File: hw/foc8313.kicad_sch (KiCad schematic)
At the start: 36 parts, among them P1 USB_C_Plug_USB2.0, SW1 SW_SPST, U1 DRV8313PWP, U2 STM32F103CBTx, U3 INA240A3D, U4 AS5047D, U5 MP2456, U6 SN65HVD230

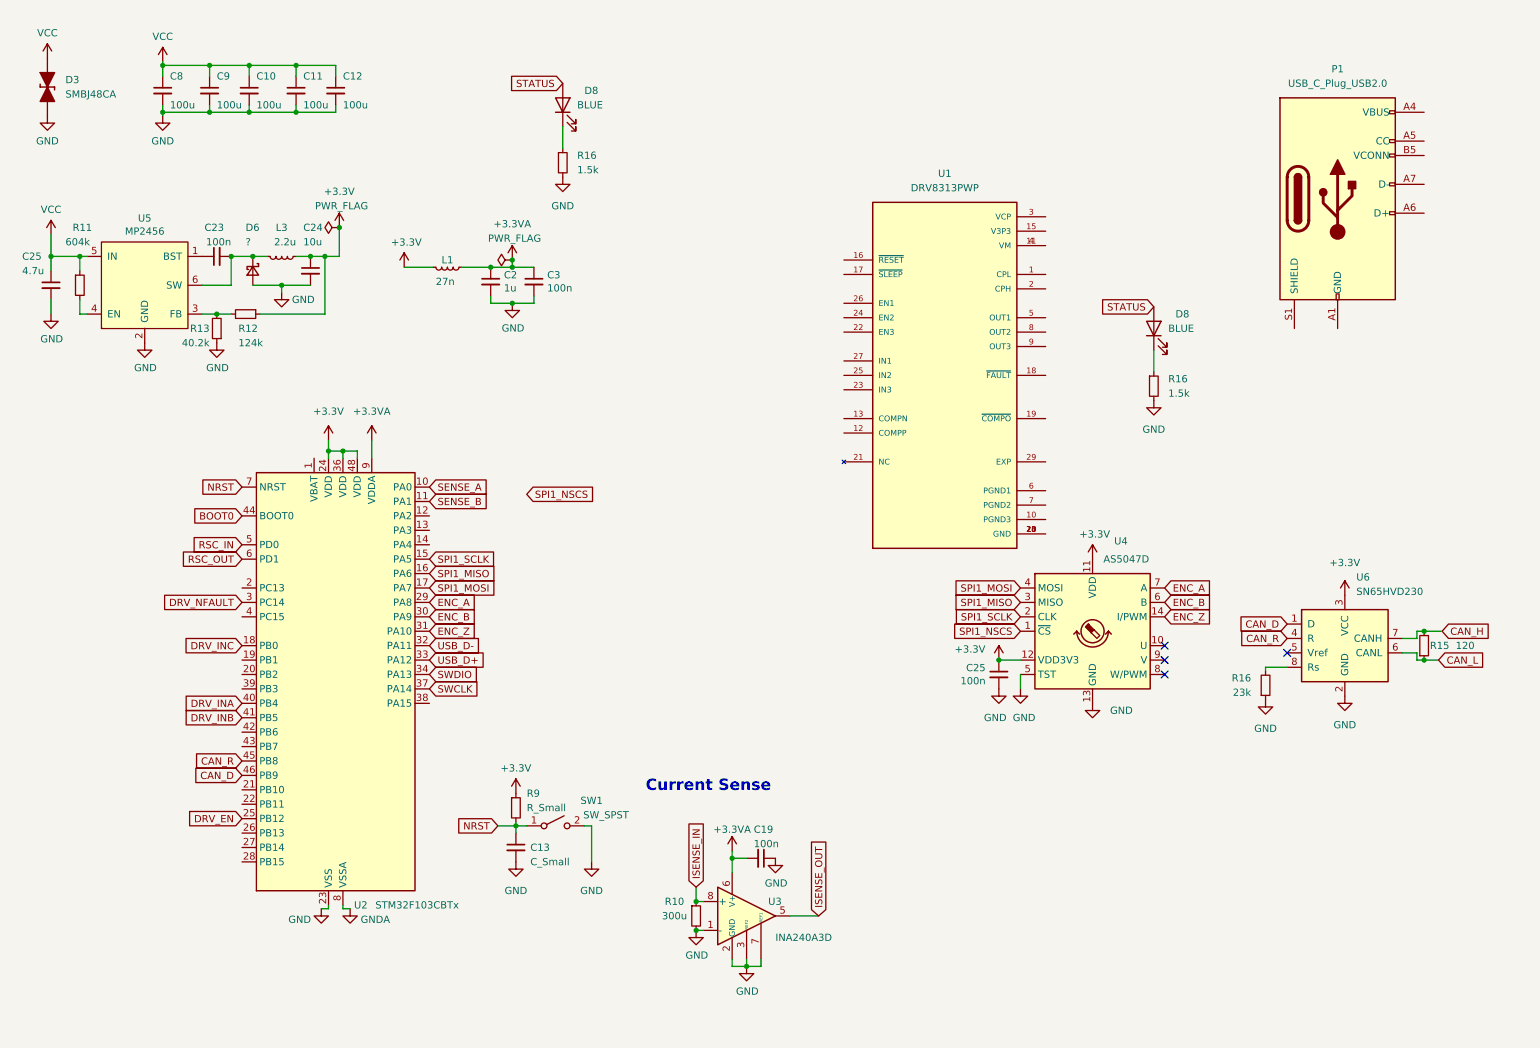
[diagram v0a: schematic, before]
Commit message: [Hw] 5V buck, Isocan, Encoder, MCU, with LCSC parts
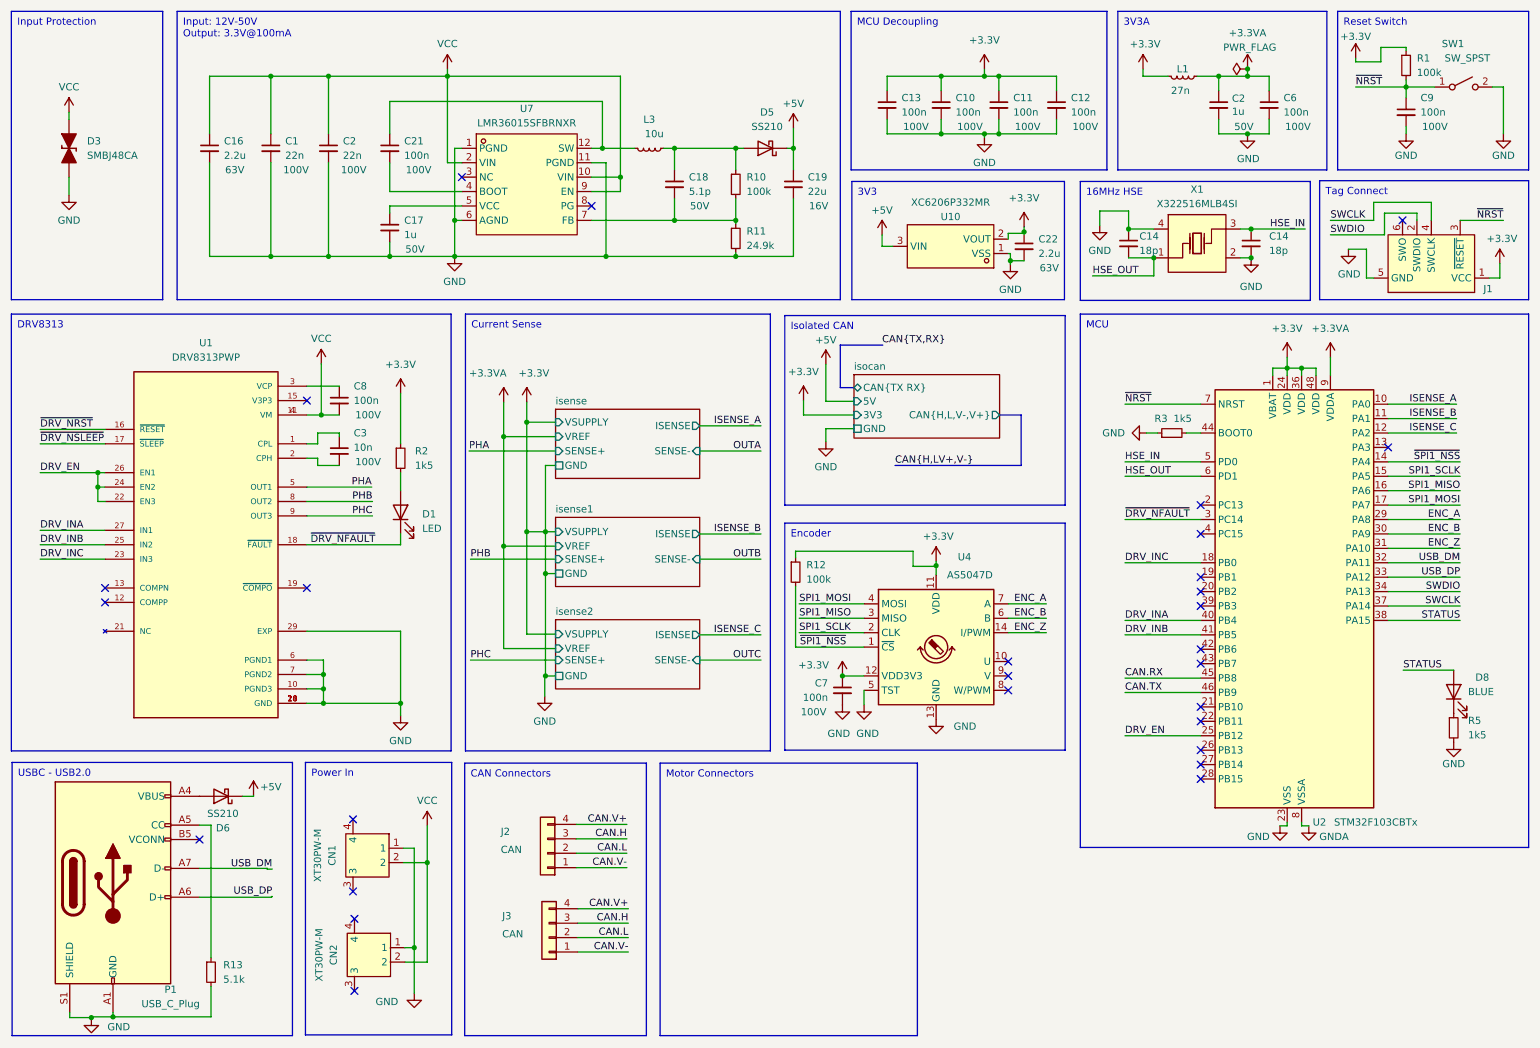
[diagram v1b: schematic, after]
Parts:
- removed C23, C25: 100n, Capacitor_SMD:C_0603_1608Metric, symbol Device:C_Small
- removed C24: 10u, Capacitor_SMD:C_0603_1608Metric, symbol Device:C_Small
- removed C25: 4.7u, Capacitor_SMD:C_0603_1608Metric, symbol Device:C_Small
- removed D6: ?, Diode_SMD:D_0603_1608Metric, symbol Device:D_Schottky_Small
- removed D8: BLUE, LED_SMD:LED_0603_1608Metric, symbol Device:LED
- removed R15: 120, Resistor_SMD:R_0805_2012Metric, symbol Device:R_Small
- removed R16: 23k, Resistor_SMD:R_0603_1608Metric, symbol Device:R_Small
- removed R16 (x2): 1.5k, Resistor_SMD:R_0603_1608Metric, symbol Device:R_Small
- removed R9: R_Small, symbol Device:R_Small
- removed U3: INA240A3D, Package_SO:SOIC-8_3.9x4.9mm_P1.27mm, symbol Amplifier_Current:INA240A3D
- removed U5: MP2456, Package_TO_SOT_SMD:TSOT-23-6, symbol MP2456:MP2456
- removed U6: SN65HVD230, Package_SO:SOIC-8_3.9x4.9mm_P1.27mm, symbol Interface_CAN_LIN:SN65HVD230
- added C1, C2: 22n, Capacitor_SMD:C_0603_1608Metric, symbol Device:C_Small
- added C14 (x2): 18p, Capacitor_SMD:C_0402_1005Metric, symbol Device:C_Small
- added C16, C22: 2.2u, Capacitor_SMD:C_0805_2012Metric, symbol Device:C_Small
- added C17: 1u, Capacitor_SMD:C_0603_1608Metric, symbol Device:C_Small
- added C18: 5.1p, Capacitor_SMD:C_0603_1608Metric, symbol Device:C_Small
- added C21, C6, C7: 100n, Capacitor_SMD:C_0603_1608Metric, symbol Device:C_Small
- added CN1, CN2: XT30PW-M, easyeda:CONN-TH_XT30PW-M, symbol easyeda:XT30PW-M
- added D1: LED, Diode_SMD:D_0603_1608Metric, symbol Device:LED
- added D5, D6: SS210, Diode_SMD:D_SMA, symbol Device:D_Schottky
- added J1: Tag Connect, Connector:Tag-Connect_TC2030-IDC-NL_2x03_P1.27mm_Vertical, symbol Connector:Conn_ARM_SWD_TagConnect_TC2030-NL
- added J2, J3: CAN, Connector_JST:JST_GH_SM04B-GHS-TB_1x04-1MP_P1.25mm_Horizontal, symbol Connector_Generic:Conn_01x04
- added R1: 100k, Resistor_SMD:R_0603_1608Metric, symbol Device:R_Small
- added R2, R3, R5: 1k5, Resistor_SMD:R_0603_1608Metric, symbol Device:R_Small
- added U10: XC6206P332MR, easyeda:SOT-23-3_L3.0-W1.7-P0.95-LS2.9-BR, symbol easyeda:XC6206P332MR_C347376
- added U7: LMR36015SFBRNXR, easyeda:VQFN-12_L3.0-W2.0-P0.65-BL_TI_RNX, symbol easyeda:LMR36015SFBRNXR
- added X1: X322516MLB4SI, easyeda:OSC-SMD_4P-L3.2-W2.5-BL, symbol easyeda:X322516MLB4SI
- C10, C11, C12, C8, C9: value 100u -> 100n; footprint (none) -> Capacitor_SMD:C_0603_1608Metric; LCSC (none) -> C15725; Rating (none) -> 100V
- C13: value C_Small -> 100n; footprint (none) -> Capacitor_SMD:C_0603_1608Metric; LCSC (none) -> C15725; Rating (none) -> 100V
- C19: value 100n -> 22u; footprint Capacitor_SMD:C_0603_1608Metric -> Resistor_SMD:R_0805_2012Metric; LCSC (none) -> C98190; Rating (none) -> 16V
- C2: LCSC (none) -> C15849; Rating (none) -> 50V
- C3: value 100n -> 10n; LCSC (none) -> C302008; Rating (none) -> 100V
- D8: LCSC (none) -> C19189746
- L1: LCSC (none) -> C280267
- L3: value 2.2u -> 10u; footprint Inductor_SMD:L_0603_1608Metric -> Inductor_SMD:L_0805_2012Metric; LCSC (none) -> C285963
- P1: value USB_C_Plug_USB2.0 -> USB_C_Plug; footprint (none) -> easyeda:USB-3.1-SMD_USB3.1-TYPE-C-FSABC
- R10: value 300u -> 100k; footprint Resistor_SMD:R_2512_6332Metric -> Resistor_SMD:R_0603_1608Metric; LCSC (none) -> C25803
- R11: value 604k -> 24.9k; LCSC (none) -> C25962
- R12: value 124k -> 100k; LCSC (none) -> C25803
- R13: value 40.2k -> 5.1k; LCSC (none) -> C23186
- U1: footprint SOP65P640X120-29N -> easyeda:HTSSOP-28_L9.8-W4.5-P0.65-LS6.6-BL-EP; LCSC (none) -> C92482
- U2: LCSC (none) -> C8304
- U4: LCSC (none) -> C962063
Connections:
- net DRV_NFAULT is gone; now on net ~{DRV_NFAULT}: U2.3 (PC14)
- net SPI1_NSCS is gone; now on net ~{SPI1_NSS}: U4.1 (~{CS})
- net USB_D+ is gone; now on net USB_DP: U2.33 (PA12)
- net USB_D- is gone; now on net USB_DM: U2.32 (PA11)
- net +3.3V: now also C10.1, C10.2, C11.1, C11.2, C12.1, C12.2, C13.1, C13.2, C19.2, C2.2, C9.2, D3.1 (K), P1.A1 (GND), P1.A12 (GND), P1.B1 (GND), P1.B12 (GND), P1.S1 (SHIELD), R11.2, R13.2, SW1.2 (B), U1.10 (PGND3), U1.14 (GND), U1.20 (GND), U1.28 (GND), U1.29 (EXP), U1.6 (PGND1), U1.7 (PGND2), U2.1 (VBAT), U2.23 (VSS), U2.35 (VSS), U2.47 (VSS), U4.13 (GND), U4.5 (TST), C1.2, C14.1, C14.2, C16.2, C17.2, C2.2, C22.1, C22.2, C6.2, C7.2, CN1.1, CN2.1, J1.5 (GND), R1.1, R2.1, R3.1, R5.2, U10.1 (VSS), U10.2 (VOUT), U7.1 (PGND), U7.11 (PGND), U7.6 (AGND), X1.2, X1.4
- net +3.3VA: now also C6.1; no longer C19.2, C3.1
- net +3V3: now also C7.1, J1.1 (VCC); no longer L3.1
- net DRV_EN: now also U1.22 (EN3), U1.24 (EN2), U1.26 (EN1)
- net DRV_INA: now also U1.27 (IN1)
- net DRV_INB: now also U1.25 (IN2)
- net DRV_INC: now also U1.23 (IN3)
- net STATUS: now also U2.38 (PA15)
- net SWCLK: now also J1.4 (SWCLK)
- net SWDIO: now also J1.2 (SWDIO)
- net VCC: now also C8.2, U1.11 (VM), U1.4 (VM), C1.1, C16.1, C2.1, CN1.2, CN2.2, U7.10 (VIN), U7.2 (VIN), U7.9 (EN); no longer C10.1, C11.1, C12.1, C8.1, C9.1, R11.1
- net ~{SPI1_NSS}: now reaches R12.2
- net ~{SPI1_NSS}: now also U2.14 (PA4); no longer R13.2
- net ISENSE_C: now reaches U2.12 (PA2)
- net at L3.2: now also C21.1, U7.12 (SW)
- net at D8.1 (K): now also R5.1
- net at U1.1 (CPL): now also C3.1
- net ~{DRV_NRST}: now reaches U1.16 (~{RESET})
- net ~{DRV_NSLEEP}: now reaches U1.17 (~{SLEEP})
- net ~{DRV_NFAULT}: now reaches U1.18 (~{FAULT})
- net ~{DRV_NFAULT}: now also D1.1 (K)
- net at U1.2 (CPH): now also C3.2
- net at U1.3 (VCP): now also C8.1
- net PHA: now reaches U1.5 (OUT1)
- net PHB: now reaches U1.8 (OUT2)
- net PHC: now reaches U1.9 (OUT3)
- net at P1.A4 (VBUS), P1.A9 (VBUS), P1.B4 (VBUS)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: now also D6.2 (A)
- net at P1.A5 (CC): now also R13.1
- net USB_DP: now reaches P1.A6 (D+)
- net USB_DM: now reaches P1.A7 (D-)
- net BOOT0: no longer names the net of U2.44 (BOOT0)
- net BOOT0: now also R3.2
- net CAN_D renamed CAN.TX
- net CAN_R renamed CAN.RX
- removed net GND: C10.2, C11.2, C12.2, C13.2, C19.1, C2.2, C3.2, C8.2, C9.2, D3.1 (K), R10.2, R13.1, SW1.2 (B), U2.23 (VSS), U2.35 (VSS), U2.47 (VSS), U4.13 (GND), U4.5 (TST)
- net ISENSE_IN: no longer names the net of R10.1
- net ISENSE_IN: now also L3.1, C18.1, D5.2 (A)
- net NRST renamed ~{NRST}
- net ~{NRST}: now also C9.1, J1.3 (~{RESET}), R1.2; no longer C13.1
- net RSC_IN renamed HSE_IN
- net HSE_IN: now also C14.1, X1.3
- net RSC_OUT renamed HSE_OUT
- net HSE_OUT: now also C14.2, X1.1
- net SENSE_A renamed ISENSE_A
- net SENSE_B renamed ISENSE_B
- new net: C18.2, R10.2, R11.1, U7.7 (FB)
- new net: C17.1, U7.5 (VCC)
- new net: D1.2 (A), R2.2
- new net: C21.2, U7.4 (BOOT)
- new net +5V: C19.1, D5.1 (K), D6.1 (K), U10.3 (VIN)
- new net CAN.H: J2.3 (Pin_3), J3.3 (Pin_3)
- new net CAN.L: J2.2 (Pin_2), J3.2 (Pin_2)
- new net CAN.V+: J2.4 (Pin_4), J3.4 (Pin_4)
- new net CAN.V-: J2.1 (Pin_1), J3.1 (Pin_1)
- no-connect marks 4 -> 28
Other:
- added sheet isense (isense.kicad_sch)
- added sheet isense1 (isense.kicad_sch)
- added sheet isense2 (isense.kicad_sch)
- added sheet isocan (isocan.kicad_sch)
- note removed: "Current Sense"
- moved on the sheet: C2, D3, D8, L1, SW1, U1, U2, U4

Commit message: WIP XT30?
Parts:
- removed J3: CAN, Connector_JST:JST_GH_SM04B-GHS-TB_1x04-1MP_P1.25mm_Horizontal, symbol Connector_Generic:Conn_01x04
- added J3: CAN, Connector_JST:JST_GH_SM03B-GHS-TB_1x03-1MP_P1.25mm_Horizontal, symbol Connector_Generic:Conn_01x03
- added U6: MR30PW-M30.G.Y, easyeda:CONN-TH_MR30PW-M30-G-Y, symbol easyeda:MR30PW-M30.G.Y
- J2: footprint Connector_JST:JST_GH_SM04B-GHS-TB_1x04-1MP_P1.25mm_Horizontal -> Connector_JST:JST_GH_SM03B-GHS-TB_1x03-1MP_P1.25mm_Horizontal; symbol Connector_Generic:Conn_01x04 -> Connector_Generic:Conn_01x03; LCSC Part C3029379 -> C514175
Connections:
- net +3.3V: no longer C1.2, C10.2, C11.2, C12.2, C13.2, C14.1, C14.2, C16.2, C17.2, C19.2, C2.2, C2.2, C22.2, C6.2, C7.2, C9.2, CN1.1, CN2.1, D3.1 (K), J1.5 (GND), P1.A1 (GND), P1.A12 (GND), P1.B1 (GND), P1.B12 (GND), P1.S1 (SHIELD), R11.2, R13.2, R3.1, R5.2, SW1.2 (B), U1.10 (PGND3), U1.14 (GND), U1.20 (GND), U1.28 (GND), U1.29 (EXP), U1.6 (PGND1), U1.7 (PGND2), U10.1 (VSS), U2.23 (VSS), U2.35 (VSS), U2.47 (VSS), U4.13 (GND), U4.5 (TST), U7.1 (PGND), U7.11 (PGND), U7.6 (AGND), X1.2, X1.4
- net CAN.H: now also J3.3 (Pin_3)
- net CAN.L: now also J3.2 (Pin_2)
- net CAN.V-: now also J3.1 (Pin_1)
- net OUTA: now also U6.1
- net OUTB: now also U6.2
- net OUTC: now also U6.3
- net VCC: now also CN1.1, CN2.1; no longer CN1.2, CN2.2
- removed net CAN.V+: J2.4 (Pin_4)
- new net GND: C1.2, C10.2, C11.2, C12.2, C13.2, C14.1, C14.2, C16.2, C17.2, C19.2, C2.2, C2.2, C22.2, C6.2, C7.2, C9.2, CN1.2, CN2.2, D3.1 (K), J1.5 (GND), P1.A1 (GND), P1.A12 (GND), P1.B1 (GND), P1.B12 (GND), P1.S1 (SHIELD), R11.2, R13.2, R3.1, R5.2, SW1.2 (B), U1.10 (PGND3), U1.14 (GND), U1.20 (GND), U1.28 (GND), U1.29 (EXP), U1.6 (PGND1), U1.7 (PGND2), U10.1 (VSS), U2.23 (VSS), U2.35 (VSS), U2.47 (VSS), U4.13 (GND), U4.5 (TST), U7.1 (PGND), U7.11 (PGND), U7.6 (AGND), X1.2, X1.4
- no-connect marks 28 -> 30

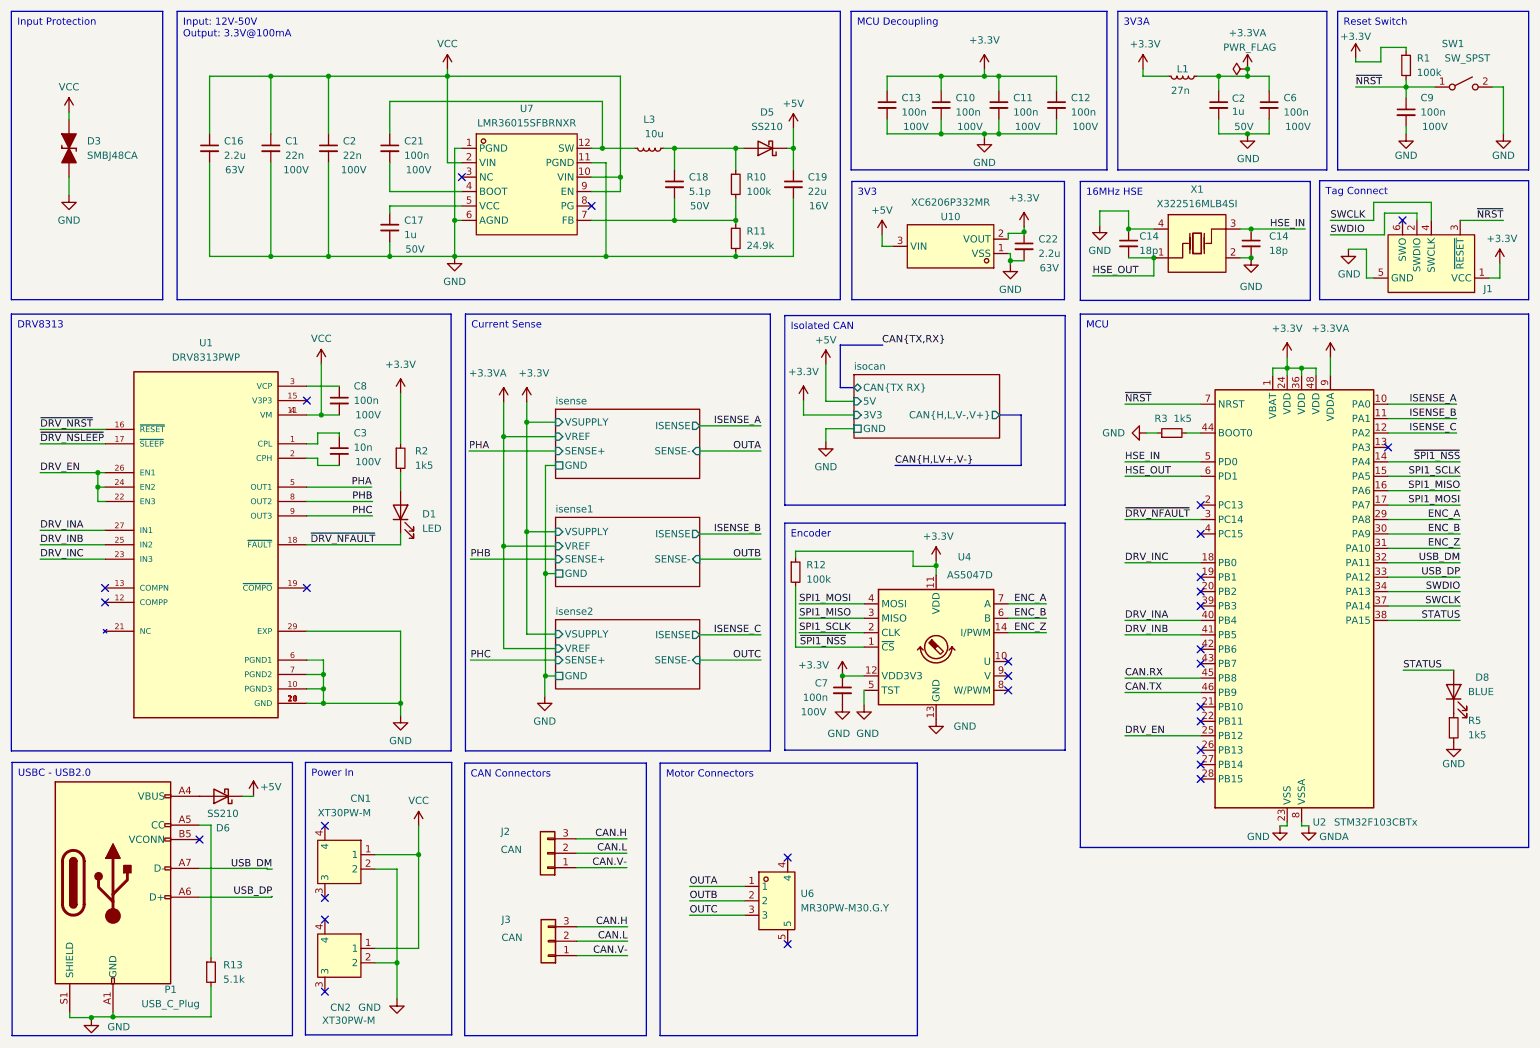
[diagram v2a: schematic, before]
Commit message: [Hw] No iso can, 0402 where possible, approx layout and formfactor
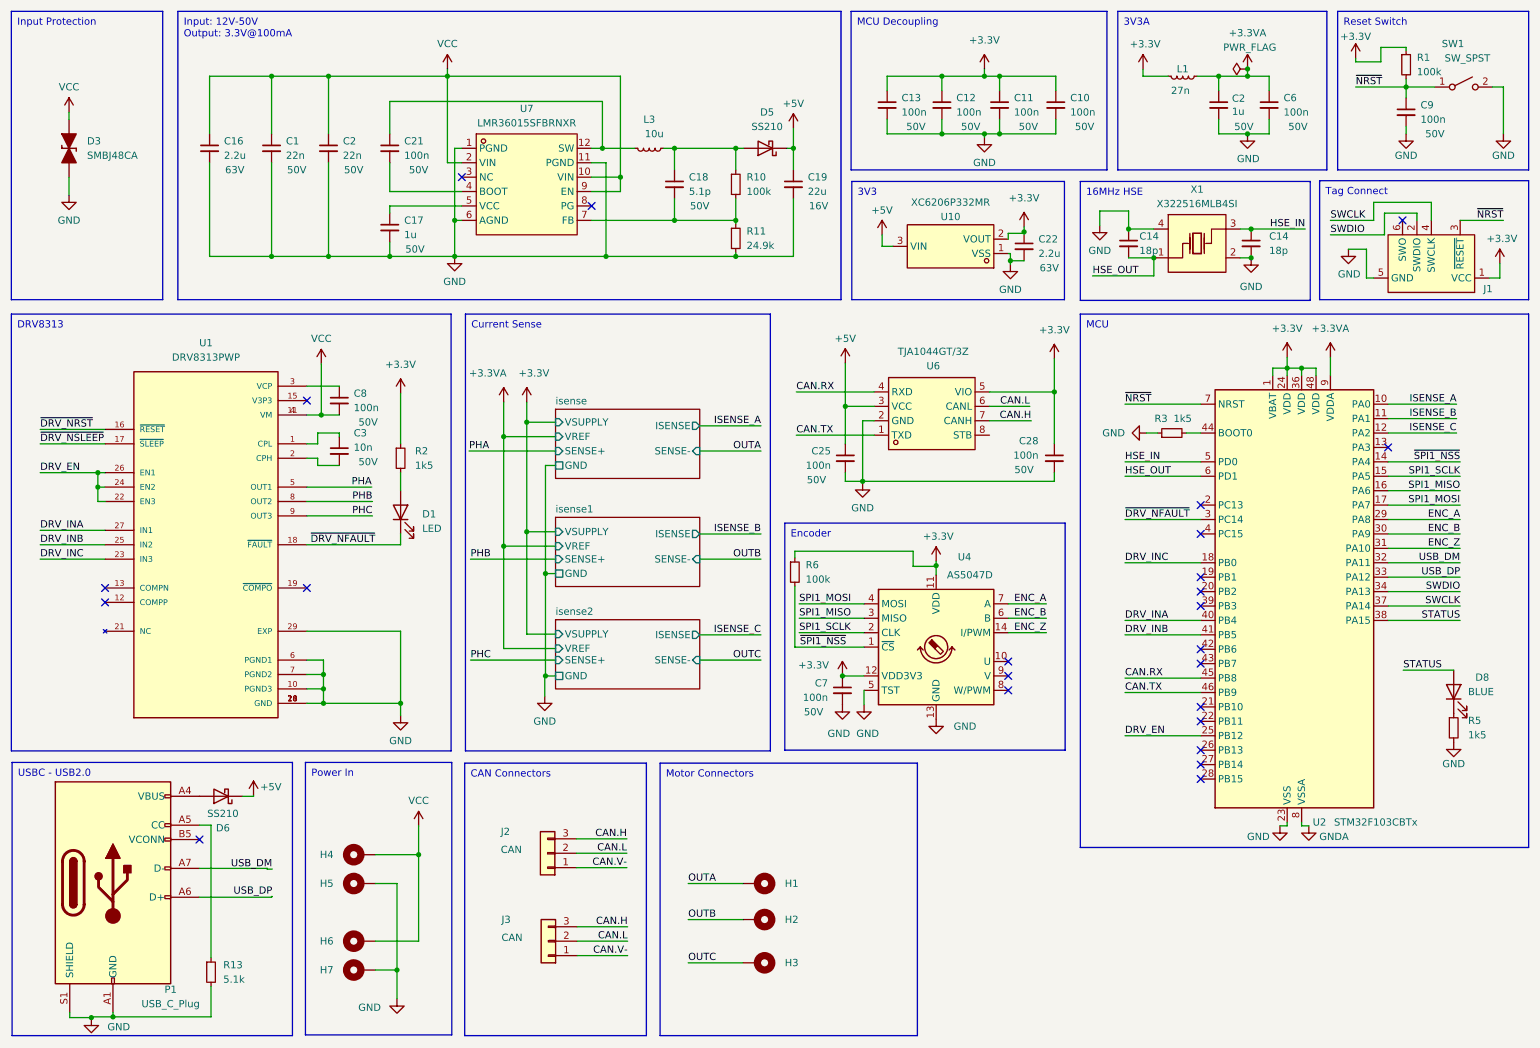
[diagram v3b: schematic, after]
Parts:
- removed CN1, CN2: XT30PW-M, easyeda:CONN-TH_XT30PW-M, symbol easyeda:XT30PW-M
- removed R12: 100k, Resistor_SMD:R_0603_1608Metric, symbol Device:R_Small
- removed U6: MR30PW-M30.G.Y, easyeda:CONN-TH_MR30PW-M30-G-Y, symbol easyeda:MR30PW-M30.G.Y
- added C25, C28: 100n, Capacitor_SMD:C_0402_1005Metric, symbol Device:C_Small
- added H1, H2, H3: MountingHole_Pad, local_lib:2x3, symbol Mechanical:MountingHole_Pad
- added H4, H5, H6, H7: MountingHole_Pad, local_lib:2x5, symbol Mechanical:MountingHole_Pad
- added R6: 100k, Resistor_SMD:R_0402_1005Metric, symbol Device:R_Small
- added U6: TJA1044GT/3Z, easyeda:SO-8_L4.9-W3.9-P1.27-LS5.9-BL, symbol easyeda:TJA1044GT_3Z
- C1, C2: footprint Capacitor_SMD:C_0603_1608Metric -> Capacitor_SMD:C_0402_1005Metric; LCSC C313105 -> C1532; Rating 100V -> 50V
- C10, C11, C12, C13, C21, C6, C7, C8, C9: footprint Capacitor_SMD:C_0603_1608Metric -> Capacitor_SMD:C_0402_1005Metric; LCSC C15725 -> C307331; Rating 100V -> 50V
- C3: footprint Capacitor_SMD:C_0603_1608Metric -> Capacitor_SMD:C_0402_1005Metric; LCSC C302008 -> C1546; Rating 100V -> 50V
- R1, R10: footprint Resistor_SMD:R_0603_1608Metric -> Resistor_SMD:R_0402_1005Metric; LCSC C25803 -> C25741
- R11: footprint Resistor_SMD:R_0603_1608Metric -> Resistor_SMD:R_0402_1005Metric; LCSC C25962 -> C138027
- R13: footprint Resistor_SMD:R_0603_1608Metric -> Resistor_SMD:R_0402_1005Metric; LCSC C23186 -> C25905
- R2, R3, R5: footprint Resistor_SMD:R_0603_1608Metric -> Resistor_SMD:R_0402_1005Metric; LCSC C22843 -> C25867
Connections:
- net +3.3V: now also C28.1, U6.5 (VIO)
- net +3V3: now also R6.1
- net +5V: now also C25.1, U6.3 (VCC)
- net CAN.H: now also U6.7 (CANH)
- net CAN.L: now also U6.6 (CANL)
- net CAN.RX: now also U6.4 (RXD)
- net CAN.TX: now also U6.1 (TXD)
- net GND: now also C25.2, C28.2, H5.1, H7.1, U6.2 (GND)
- net OUTA: now also H1.1
- net OUTB: now also H2.1
- net OUTC: now also H3.1
- net VCC: now also H4.1, H6.1
- net ~{SPI1_NSS}: now also R6.2
- no-connect marks 30 -> 24
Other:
- removed sheet isocan
